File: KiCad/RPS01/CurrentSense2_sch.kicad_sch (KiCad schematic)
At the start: 4 parts, among them U12 INA139QPWRQ1

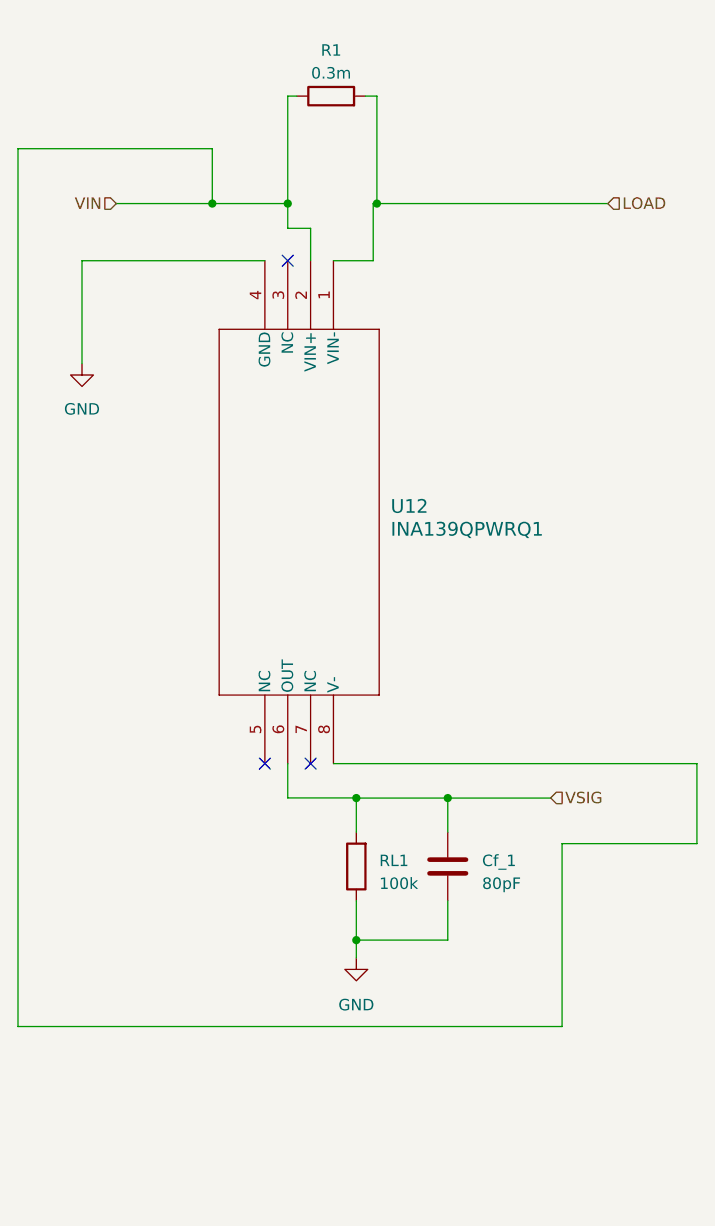
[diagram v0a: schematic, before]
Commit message: Finished most of the Schematics. Needs polishing
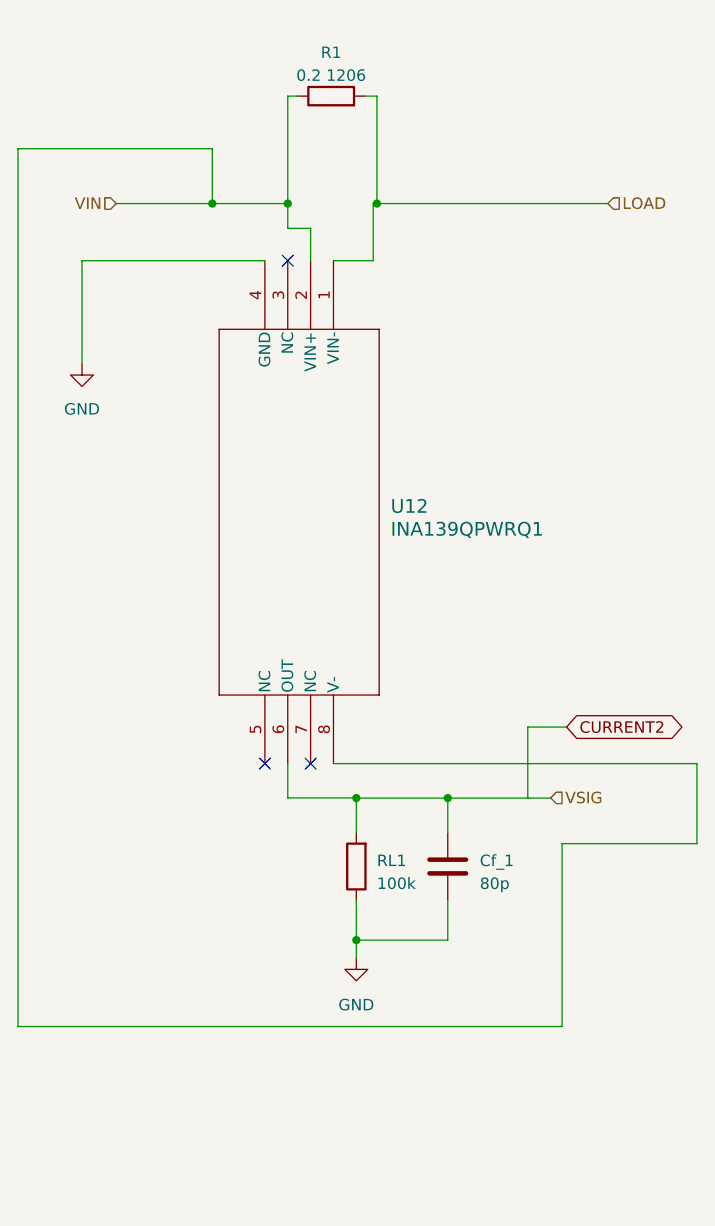
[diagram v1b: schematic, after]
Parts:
- Cf_1: value 80pF -> 80p
- R1: value 0.3m -> 0.2 1206
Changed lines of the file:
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@@
+    (stroke (width 0) (type default))
+  )
+  (wire (pts (xy 156.464 118.11) (xy 160.782 118.11))
     (stroke (width 0) (type default))
   )
@@
     (stroke (width 0) (type default))
   )
+  (wire (pts (xy 156.464 125.984) (xy 156.464 118.11))
+    (stroke (width 0) (type default))
+  )
   (wire (pts (xy 130.81 48.006) (xy 129.794 48.006))
     (stroke (width 0) (type default))
@@
   (wire (pts (xy 137.414 137.414) (xy 137.414 141.7826))
     (stroke (width 0) (type default))
+  )
+  (global_label "CURRENT2" (shape bidirectional) (at 160.782 118.11 0) (fields_autoplaced)
+    (effects (font (size 1.27 1.27)) (justify left))
+    (property "Intersheetrefs" "${INTERSHEET_REFS}" (at 174.5962 118.11 0)
+      (effects (font (size 1.27 1.27)) (justify left) hide)
+    )
   )
   (hierarchical_label "VSIG" (shape input) (at 159.004 125.984 0) (fields_autoplaced)
@@
         )
         (path "/14930f15-c0a0-4b55-93e6-b112548415f6/83d3dc76-6aeb-422d-8708-14a32de244f0"
-          (reference "#PWR041") (unit 1)
+          (reference "#PWR052") (unit 1)
         )
       )
@@
   (symbol (lib_id "Device:R") (at 137.414 133.604 180) (unit 1)
     (in_bom yes) (on_board yes) (dnp no) (fields_autoplaced)
-    (property "Reference" "RL1" (at 139.954 132.969 0)
+    (property "Reference" "RL1" (at 139.7 132.969 0)
       (effects (font (size 1.27 1.27)) (justify right))
     )
-    (property "Value" "100k" (at 139.954 135.509 0)
+    (property "Value" "100k" (at 139.7 135.509 0)
       (effects (font (size 1.27 1.27)) (justify right))
     )
@@
         )
         (path "/14930f15-c0a0-4b55-93e6-b112548415f6/83d3dc76-6aeb-422d-8708-14a32de244f0"
-          (reference "RL2") (unit 1)
+          (reference "R22") (unit 1)
         )
       )
@@
         )
         (path "/14930f15-c0a0-4b55-93e6-b112548415f6/83d3dc76-6aeb-422d-8708-14a32de244f0"
-          (reference "U7") (unit 1)
+          (reference "U16") (unit 1)
         )
       )
@@
   (symbol (lib_id "Device:R") (at 134.62 48.006 90) (unit 1)
     (in_bom yes) (on_board yes) (dnp no) (fields_autoplaced)
-    (property "Reference" "R1" (at 134.62 42.926 90)
-      (effects (font (size 1.27 1.27)))
-    )
-    (property "Value" "0.3m" (at 134.62 45.466 90)
+    (property "Reference" "R1" (at 134.62 43.18 90)
+      (effects (font (size 1.27 1.27)))
+    )
+    (property "Value" "0.2 1206" (at 134.62 45.72 90)
       (effects (font (size 1.27 1.27)))
     )
@@
         )
         (path "/14930f15-c0a0-4b55-93e6-b112548415f6/83d3dc76-6aeb-422d-8708-14a32de244f0"
-          (reference "R7") (unit 1)
+          (reference "R27") (unit 1)
         )
       )
@@
   (symbol (lib_id "Device:C") (at 147.574 133.604 0) (unit 1)
     (in_bom yes) (on_board yes) (dnp no) (fields_autoplaced)
-    (property "Reference" "Cf_1" (at 151.384 132.969 0)
+    (property "Reference" "Cf_1" (at 151.13 132.969 0)
       (effects (font (size 1.27 1.27)) (justify left))
     )
-    (property "Value" "80pF" (at 151.384 135.509 0)
+    (property "Value" "80p" (at 151.13 135.509 0)
       (effects (font (size 1.27 1.27)) (justify left))
     )
@@
         )
         (path "/14930f15-c0a0-4b55-93e6-b112548415f6/83d3dc76-6aeb-422d-8708-14a32de244f0"
-          (reference "Cf_2") (unit 1)
+          (reference "C24") (unit 1)
         )
       )
@@
         )
         (path "/14930f15-c0a0-4b55-93e6-b112548415f6/83d3dc76-6aeb-422d-8708-14a32de244f0"
-          (reference "#PWR039") (unit 1)
-        )
-      )
+          (reference "#PWR051") (unit 1)
+        )
+      )

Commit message: Finished Updating Footprints and Reorganized Reference Designators
Finished Updating Footprints and Reorganized Reference Designators

Starting to work on Final PCB, except for 19V Boost. Please check Schematic for errors
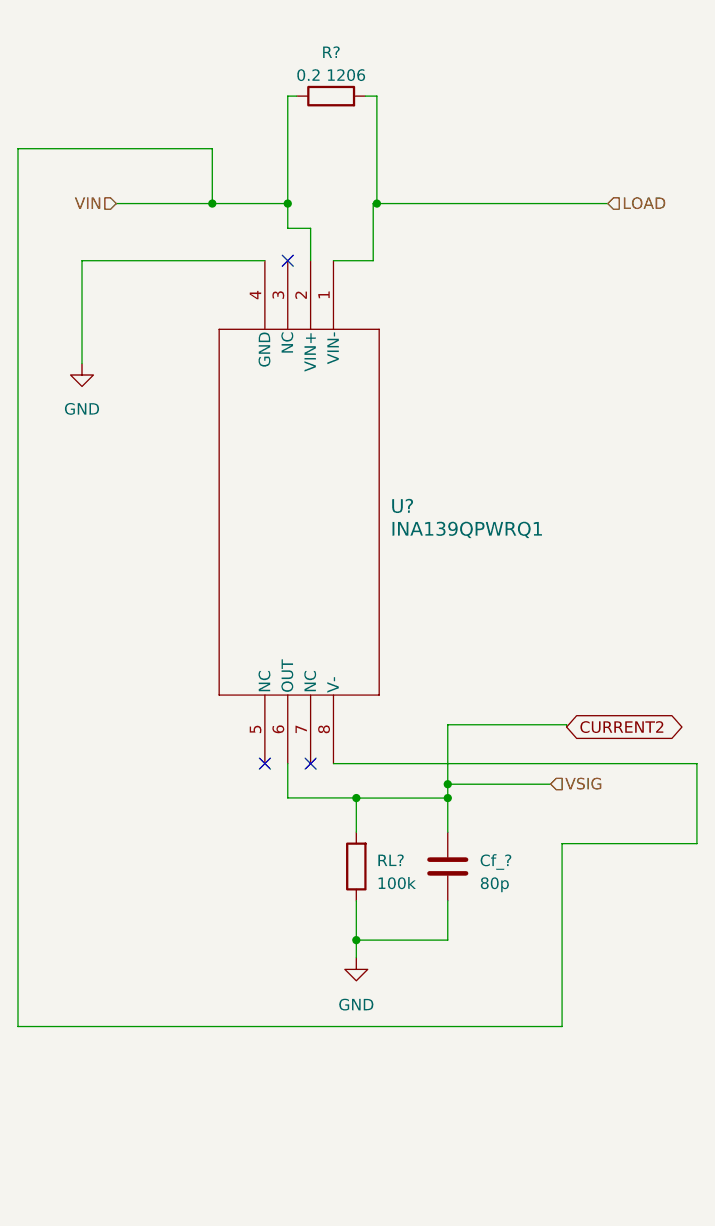
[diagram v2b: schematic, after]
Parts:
- renumbered Cf_1 to Cf_?, R1 to R?, RL1 to RL?, U12 to U?
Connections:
- net VSIG is gone; now on net CURRENT2: Cf_?.1, RL?.2, U?.6 (OUT)
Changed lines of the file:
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@@
   (junction (at 129.794 59.944) (diameter 0) (color 0 0 0 0)
+  )
+  (junction (at 147.574 124.46) (diameter 0) (color 0 0 0 0)
   )
   (junction (at 137.414 141.7826) (diameter 0) (color 0 0 0 0)
@@
     (stroke (width 0) (type default))
   )
-  (wire (pts (xy 156.464 118.11) (xy 160.782 118.11))
-    (stroke (width 0) (type default))
-  )
   (wire (pts (xy 137.414 125.9998) (xy 147.574 125.9998))
     (stroke (width 0) (type default))
@@
     (stroke (width 0) (type default))
   )
-  (wire (pts (xy 147.574 125.9998) (xy 159.004 125.9998))
+  (wire (pts (xy 147.574 124.46) (xy 159.004 124.46))
     (stroke (width 0) (type default))
   )
@@
     (stroke (width 0) (type default))
   )
+  (wire (pts (xy 160.782 117.856) (xy 160.782 118.11))
+    (stroke (width 0) (type default))
+  )
   (wire (pts (xy 137.414 125.984) (xy 137.414 125.9998))
     (stroke (width 0) (type default))
   )
+  (wire (pts (xy 147.574 117.856) (xy 160.782 117.856))
+    (stroke (width 0) (type default))
+  )
   (wire (pts (xy 139.7 59.944) (xy 165.354 59.944))
     (stroke (width 0) (type default))
   )
+  (wire (pts (xy 147.574 124.46) (xy 147.574 125.9998))
+    (stroke (width 0) (type default))
+  )
   (wire (pts (xy 147.574 141.7826) (xy 137.414 141.7826))
     (stroke (width 0) (type default))
@@
     (stroke (width 0) (type default))
   )
-  (wire (pts (xy 156.464 125.984) (xy 156.464 118.11))
-    (stroke (width 0) (type default))
-  )
   (wire (pts (xy 130.81 48.006) (xy 129.794 48.006))
     (stroke (width 0) (type default))
@@
     (stroke (width 0) (type default))
   )
+  (wire (pts (xy 147.574 124.46) (xy 147.574 117.856))
+    (stroke (width 0) (type default))
+  )
   (wire (pts (xy 139.7 48.006) (xy 139.7 59.944))
     (stroke (width 0) (type default))
   )
-  (wire (pts (xy 159.004 125.9998) (xy 159.004 125.984))
+  (wire (pts (xy 159.004 124.46) (xy 159.004 124.4442))
     (stroke (width 0) (type default))
   )
@@
     )
   )
-  (hierarchical_label "VSIG" (shape input) (at 159.004 125.984 0) (fields_autoplaced)
+  (hierarchical_label "VSIG" (shape input) (at 159.004 124.4442 0) (fields_autoplaced)
     (effects (font (size 1.27 1.27)) (justify left))
   )
@@
   (symbol (lib_id "power:GND") (at 137.414 143.764 0) (unit 1)
     (in_bom yes) (on_board yes) (dnp no) (fields_autoplaced)
-    (property "Reference" "#PWR040" (at 137.414 150.114 0)
+    (property "Reference" "#PWR?" (at 137.414 150.114 0)
       (effects (font (size 1.27 1.27)) hide)
     )
@@
       (project "rps01"
         (path "/14930f15-c0a0-4b55-93e6-b112548415f6/13e150ee-6c46-47a5-9c09-3749eb0dcbfe"
-          (reference "#PWR040") (unit 1)
-        )
-        (path "/14930f15-c0a0-4b55-93e6-b112548415f6/83d3dc76-6aeb-422d-8708-14a32de244f0"
-          (reference "#PWR052") (unit 1)
+          (reference "#PWR?") (unit 1)
+        )
+        (path "/14930f15-c0a0-4b55-93e6-b112548415f6/83d3dc76-6aeb-422d-8708-14a32de244f0"
+          (reference "#PWR054") (unit 1)
         )
       )
@@
   (symbol (lib_id "Device:R") (at 137.414 133.604 180) (unit 1)
     (in_bom yes) (on_board yes) (dnp no) (fields_autoplaced)
-    (property "Reference" "RL1" (at 139.7 132.969 0)
+    (property "Reference" "RL?" (at 139.7 132.969 0)
       (effects (font (size 1.27 1.27)) (justify right))
     )
@@
       (project "rps01"
         (path "/14930f15-c0a0-4b55-93e6-b112548415f6/13e150ee-6c46-47a5-9c09-3749eb0dcbfe"
-          (reference "RL1") (unit 1)
-        )
-        (path "/14930f15-c0a0-4b55-93e6-b112548415f6/83d3dc76-6aeb-422d-8708-14a32de244f0"
-          (reference "R22") (unit 1)
+          (reference "RL?") (unit 1)
+        )
+        (path "/14930f15-c0a0-4b55-93e6-b112548415f6/83d3dc76-6aeb-422d-8708-14a32de244f0"
+          (reference "R33") (unit 1)
         )
       )
@@
   (symbol (lib_id "INA139:INA139QPWRQ1") (at 134.874 66.294 270) (unit 1)
     (in_bom yes) (on_board yes) (dnp no) (fields_autoplaced)
-    (property "Reference" "U12" (at 141.224 93.599 90)
+    (property "Reference" "U?" (at 141.224 93.599 90)
       (effects (font (size 1.524 1.524)) (justify left))
     )
@@
       (project "rps01"
         (path "/14930f15-c0a0-4b55-93e6-b112548415f6/13e150ee-6c46-47a5-9c09-3749eb0dcbfe"
-          (reference "U12") (unit 1)
-        )
-        (path "/14930f15-c0a0-4b55-93e6-b112548415f6/83d3dc76-6aeb-422d-8708-14a32de244f0"
-          (reference "U16") (unit 1)
+          (reference "U?") (unit 1)
+        )
+        (path "/14930f15-c0a0-4b55-93e6-b112548415f6/83d3dc76-6aeb-422d-8708-14a32de244f0"
+          (reference "U18") (unit 1)
         )
       )
@@
   (symbol (lib_id "Device:R") (at 134.62 48.006 90) (unit 1)
     (in_bom yes) (on_board yes) (dnp no) (fields_autoplaced)
-    (property "Reference" "R1" (at 134.62 43.18 90)
+    (property "Reference" "R?" (at 134.62 43.18 90)
       (effects (font (size 1.27 1.27)))
     )
@@
       (project "rps01"
         (path "/14930f15-c0a0-4b55-93e6-b112548415f6/13e150ee-6c46-47a5-9c09-3749eb0dcbfe"
-          (reference "R1") (unit 1)
-        )
-        (path "/14930f15-c0a0-4b55-93e6-b112548415f6/83d3dc76-6aeb-422d-8708-14a32de244f0"
-          (reference "R27") (unit 1)
+          (reference "R?") (unit 1)
+        )
+        (path "/14930f15-c0a0-4b55-93e6-b112548415f6/83d3dc76-6aeb-422d-8708-14a32de244f0"
+          (reference "R32") (unit 1)
         )
       )
@@
   (symbol (lib_id "Device:C") (at 147.574 133.604 0) (unit 1)
     (in_bom yes) (on_board yes) (dnp no) (fields_autoplaced)
-    (property "Reference" "Cf_1" (at 151.13 132.969 0)
+    (property "Reference" "Cf_?" (at 151.13 132.969 0)
       (effects (font (size 1.27 1.27)) (justify left))
     )
@@
       (project "rps01"
         (path "/14930f15-c0a0-4b55-93e6-b112548415f6/13e150ee-6c46-47a5-9c09-3749eb0dcbfe"
-          (reference "Cf_1") (unit 1)
-        )
-        (path "/14930f15-c0a0-4b55-93e6-b112548415f6/83d3dc76-6aeb-422d-8708-14a32de244f0"
-          (reference "C24") (unit 1)
+          (reference "Cf_?") (unit 1)
+        )
+        (path "/14930f15-c0a0-4b55-93e6-b112548415f6/83d3dc76-6aeb-422d-8708-14a32de244f0"
+          (reference "C13") (unit 1)
         )
       )
@@
   (symbol (lib_id "power:GND") (at 106.934 77.724 0) (unit 1)
     (in_bom yes) (on_board yes) (dnp no) (fields_autoplaced)
-    (property "Reference" "#PWR030" (at 106.934 84.074 0)
+    (property "Reference" "#PWR?" (at 106.934 84.074 0)
       (effects (font (size 1.27 1.27)) hide)
     )
@@
       (project "rps01"
         (path "/14930f15-c0a0-4b55-93e6-b112548415f6/13e150ee-6c46-47a5-9c09-3749eb0dcbfe"
-          (reference "#PWR030") (unit 1)
-        )
-        (path "/14930f15-c0a0-4b55-93e6-b112548415f6/83d3dc76-6aeb-422d-8708-14a32de244f0"
-          (reference "#PWR051") (unit 1)
-        )
-      )
+          (reference "#PWR?") (unit 1)
+        )
+        (path "/14930f15-c0a0-4b55-93e6-b112548415f6/83d3dc76-6aeb-422d-8708-14a32de244f0"
+          (reference "#PWR053") (unit 1)
+        )
+      )

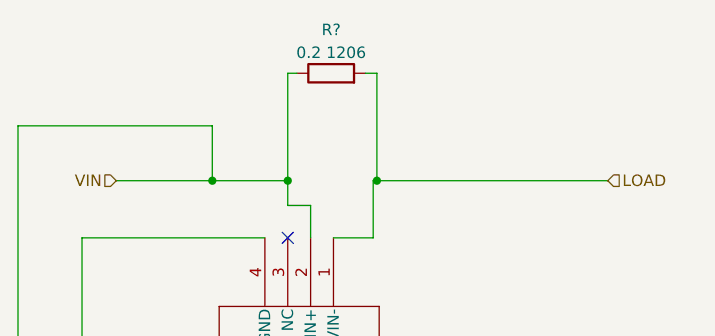
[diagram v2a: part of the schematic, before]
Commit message: Board Ready For layout. Except for 19V Boost? CHECK vs SIM Please
Board Ready For layout. Except for 19V Boost? CHECK vs SIM Please
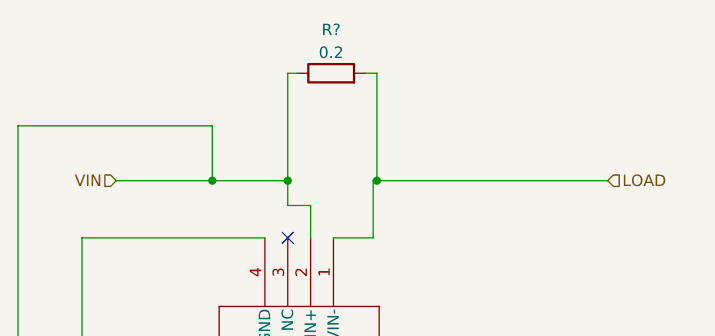
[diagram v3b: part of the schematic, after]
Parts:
- R?: value 0.2 1206 -> 0.2; footprint Mechatronic Footprints:CSS2H-5930R -> Resistor_SMD:R_1206_3216Metric
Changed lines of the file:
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@@
         )
         (path "/14930f15-c0a0-4b55-93e6-b112548415f6/83d3dc76-6aeb-422d-8708-14a32de244f0"
-          (reference "#PWR054") (unit 1)
+          (reference "#PWR079") (unit 1)
         )
       )
@@
         )
         (path "/14930f15-c0a0-4b55-93e6-b112548415f6/83d3dc76-6aeb-422d-8708-14a32de244f0"
-          (reference "R33") (unit 1)
+          (reference "R31") (unit 1)
         )
       )
@@
         )
         (path "/14930f15-c0a0-4b55-93e6-b112548415f6/83d3dc76-6aeb-422d-8708-14a32de244f0"
-          (reference "U18") (unit 1)
+          (reference "U19") (unit 1)
         )
       )
@@
       (effects (font (size 1.27 1.27)))
     )
-    (property "Value" "0.2 1206" (at 134.62 45.72 90)
+    (property "Value" "0.2" (at 134.62 45.72 90)
       (effects (font (size 1.27 1.27)))
     )
-    (property "Footprint" "Mechatronic Footprints:CSS2H-5930R" (at 134.62 49.784 90)
+    (property "Footprint" "Resistor_SMD:R_1206_3216Metric" (at 134.62 49.784 90)
       (effects (font (size 1.27 1.27)) hide)
     )
@@
         )
         (path "/14930f15-c0a0-4b55-93e6-b112548415f6/83d3dc76-6aeb-422d-8708-14a32de244f0"
-          (reference "R32") (unit 1)
+          (reference "R_S4") (unit 1)
         )
       )
@@
         )
         (path "/14930f15-c0a0-4b55-93e6-b112548415f6/83d3dc76-6aeb-422d-8708-14a32de244f0"
-          (reference "C13") (unit 1)
+          (reference "C22") (unit 1)
         )
       )
@@
         )
         (path "/14930f15-c0a0-4b55-93e6-b112548415f6/83d3dc76-6aeb-422d-8708-14a32de244f0"
-          (reference "#PWR053") (unit 1)
+          (reference "#PWR078") (unit 1)
         )
       )

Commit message: Updates
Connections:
- net LOAD: now also U?.2 (VIN+), U?.8 (V-); no longer R?.2
- removed net VIN: R?.1, U?.2 (VIN+), U?.8 (V-)
- no-connect marks 3 -> 5
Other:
- moved on the sheet: R?
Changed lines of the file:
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@@
 (kicad_sch (version 20230121) (generator eeschema)
   (paper "A4")
-  (junction (at 129.794 59.944) (diameter 0) (color 0 0 0 0)
-  )
   (junction (at 147.574 124.46) (diameter 0) (color 0 0 0 0)
   )
@@
   (junction (at 139.7 59.944) (diameter 0) (color 0 0 0 0)
   )
+  (junction (at 128.524 59.944) (diameter 0) (color 0 0 0 0)
+  )
   (junction (at 137.414 125.9998) (diameter 0) (color 0 0 0 0)
   )
   (junction (at 121.412 59.944) (diameter 0) (color 0 0 0 0)
   )
+  (no_connect (at 137.922 45.974))
   (no_connect (at 127.254 122.174))
   (no_connect (at 129.794 66.294))
   (no_connect (at 132.334 122.174))
+  (no_connect (at 130.302 45.974))
+  (wire (pts (xy 128.524 59.944) (xy 129.794 59.944))
+    (stroke (width 0) (type default))
+  )
   (wire (pts (xy 129.794 125.984) (xy 137.414 125.984))
     (stroke (width 0) (type default))
@@
     (stroke (width 0) (type default))
   )
+  (wire (pts (xy 128.524 48.006) (xy 139.7 48.006))
+    (stroke (width 0) (type default))
+  )
   (wire (pts (xy 129.794 122.174) (xy 129.794 125.984))
     (stroke (width 0) (type default))
@@
     (stroke (width 0) (type default))
   )
-  (wire (pts (xy 138.43 48.006) (xy 139.7 48.006))
-    (stroke (width 0) (type default))
-  )
   (wire (pts (xy 139.2882 59.944) (xy 139.2882 66.294))
     (stroke (width 0) (type default))
@@
     (stroke (width 0) (type default))
   )
-  (wire (pts (xy 121.412 59.944) (xy 129.794 59.944))
-    (stroke (width 0) (type default))
-  )
-  (wire (pts (xy 130.81 48.006) (xy 129.794 48.006))
+  (wire (pts (xy 121.412 59.944) (xy 128.524 59.944))
     (stroke (width 0) (type default))
   )
@@
     (stroke (width 0) (type default))
   )
-  (wire (pts (xy 129.794 48.006) (xy 129.794 59.944))
-    (stroke (width 0) (type default))
-  )
   (wire (pts (xy 99.822 53.848) (xy 121.412 53.848))
+    (stroke (width 0) (type default))
+  )
+  (wire (pts (xy 128.524 59.944) (xy 128.524 48.006))
     (stroke (width 0) (type default))
   )
@@
     )
   )
-  (symbol (lib_id "Device:R") (at 134.62 48.006 90) (unit 1)
-    (in_bom yes) (on_board yes) (dnp no) (fields_autoplaced)
-    (property "Reference" "R?" (at 134.62 43.18 90)
+  (symbol (lib_id "Device:R") (at 134.112 45.974 90) (unit 1)
+    (in_bom yes) (on_board yes) (dnp no)
+    (property "Reference" "R?" (at 134.112 41.148 90)
       (effects (font (size 1.27 1.27)))
     )
-    (property "Value" "0.2" (at 134.62 45.72 90)
+    (property "Value" "0.2" (at 133.858 43.688 90)
       (effects (font (size 1.27 1.27)))
     )
-    (property "Footprint" "Resistor_SMD:R_1206_3216Metric" (at 134.62 49.784 90)
-      (effects (font (size 1.27 1.27)) hide)
-    )
-    (property "Datasheet" "~" (at 134.62 48.006 0)
-      (effects (font (size 1.27 1.27)) hide)
-    )
+    (property "Footprint" "Resistor_SMD:R_1206_3216Metric" (at 134.112 47.752 90)
+      (effects (font (size 1.27 1.27)) hide)
+    )
+    (property "Datasheet" "~" (at 134.112 45.974 0)
+      (effects (font (size 1.27 1.27)) hide)
+    )
